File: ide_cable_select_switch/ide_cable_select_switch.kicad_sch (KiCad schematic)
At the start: 4 parts, among them J1 Conn_02x20_Odd_Even, J2 Conn_02x20_Odd_Even, J3 Conn_02x20_Odd_Even, SW1 SW_SPDT

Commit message: Updated headers in to specific IDE header without pad for key pin
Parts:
- J1, J2, J3: footprint Connector_PinHeader_2.54mm:PinHeader_2x20_P2.54mm_Vertical_SMD -> (none)
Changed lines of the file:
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@@
     (property "Reference" "J2" (id 0) (at 177.8 97.79 0))
     (property "Value" "Conn_02x20_Odd_Even" (id 1) (at 177.8 100.33 0))
-    (property "Footprint" "Connector_PinHeader_2.54mm:PinHeader_2x20_P2.54mm_Vertical_SMD" (id 2) (at 176.53 127 0)
+    (property "Footprint" "" (id 2) (at 176.53 127 0)
       (effects (font (size 1.27 1.27)) hide)
     )
@@
     (property "Reference" "J1" (id 0) (at 127 96.52 0))
     (property "Value" "Conn_02x20_Odd_Even" (id 1) (at 127 99.06 0))
-    (property "Footprint" "Connector_PinHeader_2.54mm:PinHeader_2x20_P2.54mm_Vertical_SMD" (id 2) (at 125.73 125.73 0)
+    (property "Footprint" "" (id 2) (at 125.73 125.73 0)
       (effects (font (size 1.27 1.27)) hide)
     )
@@
     (property "Reference" "J3" (id 0) (at 228.6 97.79 0))
     (property "Value" "Conn_02x20_Odd_Even" (id 1) (at 228.6 100.33 0))
-    (property "Footprint" "Connector_PinHeader_2.54mm:PinHeader_2x20_P2.54mm_Vertical_SMD" (id 2) (at 227.33 127 0)
+    (property "Footprint" "" (id 2) (at 227.33 127 0)
       (effects (font (size 1.27 1.27)) hide)
     )
@@
   (symbol_instances
     (path "/81a8578d-4991-432e-90c5-863c1508a25f"
-      (reference "J1") (unit 1) (value "Conn_02x20_Odd_Even") (footprint "Connector_PinHeader_2.54mm:PinHeader_2x20_P2.54mm_Vertical_SMD")
+      (reference "J1") (unit 1) (value "Conn_02x20_Odd_Even") (footprint "ide_cable_select_switch:IDE_ATA_Male_2x20_P2.54mm_Vertical_SMD")
     )
     (path "/2725ff94-5a7c-47c5-8447-1ffd34b9328e"
-      (reference "J2") (unit 1) (value "Conn_02x20_Odd_Even") (footprint "Connector_PinHeader_2.54mm:PinHeader_2x20_P2.54mm_Vertical_SMD")
+      (reference "J2") (unit 1) (value "Conn_02x20_Odd_Even") (footprint "ide_cable_select_switch:IDE_ATA_Male_2x20_P2.54mm_Vertical_SMD")
     )
     (path "/d0fe8934-21c4-4e46-b5b6-40801fb05422"
-      (reference "J3") (unit 1) (value "Conn_02x20_Odd_Even") (footprint "Connector_PinHeader_2.54mm:PinHeader_2x20_P2.54mm_Vertical_SMD")
+      (reference "J3") (unit 1) (value "Conn_02x20_Odd_Even") (footprint "ide_cable_select_switch:IDE_ATA_Male_2x20_P2.54mm_Vertical_SMD")
     )
     (path "/f84f0aad-79f2-4bd7-bb35-f56f8e0ea461"

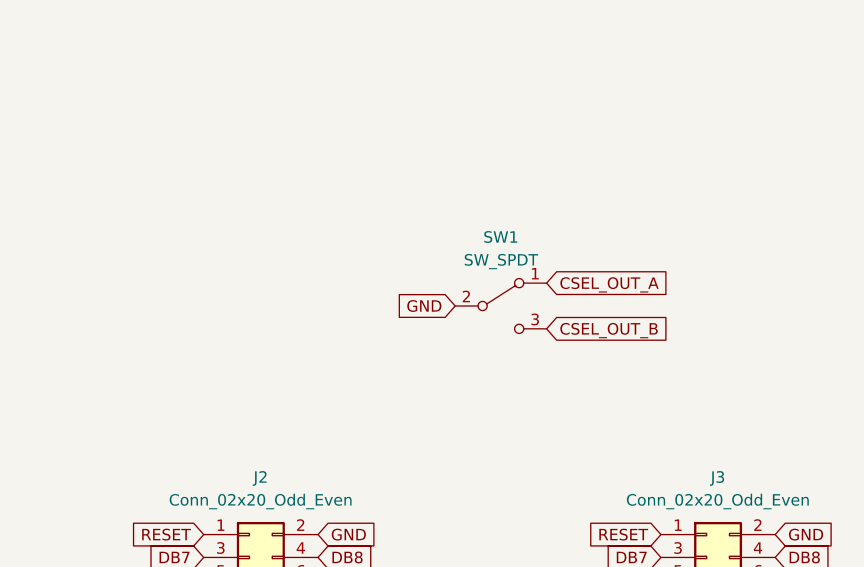
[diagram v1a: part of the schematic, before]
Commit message: Add pads for external switch
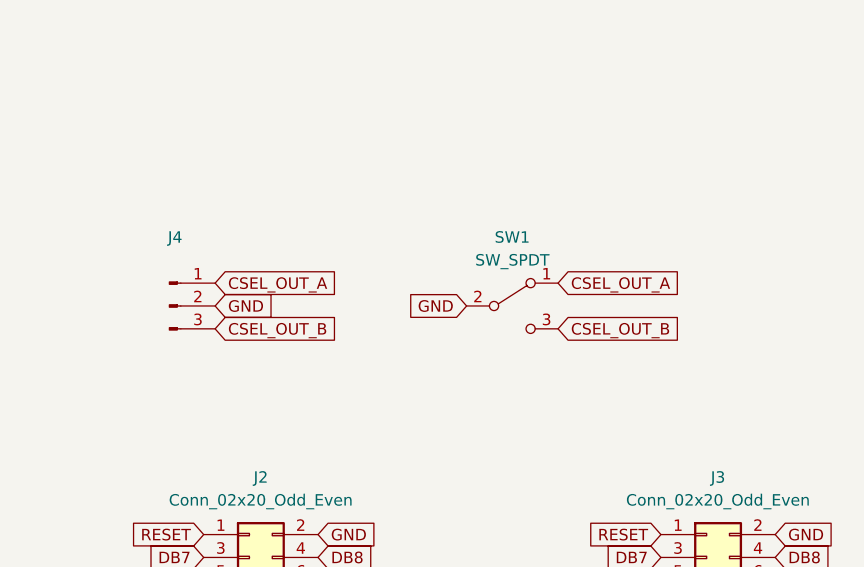
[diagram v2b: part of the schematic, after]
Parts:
- added J4: (no value), symbol Connector:Conn_01x03_Male
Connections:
- net CSEL_OUT_A: now also J4.1 (Pin_1)
- net CSEL_OUT_B: now also J4.3 (Pin_3)
- net GND: now also J4.2 (Pin_2)
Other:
- moved on the sheet: SW1
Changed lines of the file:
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@@
     )
   )
-  (global_label "CSEL_OUT_A" (shape input) (at 209.55 76.2 0) (fields_autoplaced)
-    (effects (font (size 1.27 1.27)) (justify left))
-    (property "Intersheet References" "${INTERSHEET_REFS}" (id 0) (at 223.2721 76.1206 0)
+  (global_label "CSEL_OUT_A" (shape input) (at 210.82 76.2 0) (fields_autoplaced)
+    (effects (font (size 1.27 1.27)) (justify left))
+    (property "Intersheet References" "${INTERSHEET_REFS}" (id 0) (at 224.5421 76.1206 0)
       (effects (font (size 1.27 1.27)) (justify left) hide)
     )
@@
     )
   )
+  (global_label "CSEL_OUT_B" (shape input) (at 210.82 81.28 0) (fields_autoplaced)
+    (effects (font (size 1.27 1.27)) (justify left))
+    (property "Intersheet References" "${INTERSHEET_REFS}" (id 0) (at 224.7236 81.2006 0)
+      (effects (font (size 1.27 1.27)) (justify left) hide)
+    )
+  )
+  (global_label "CSEL_OUT_A" (shape input) (at 172.72 76.2 0) (fields_autoplaced)
+    (effects (font (size 1.27 1.27)) (justify left))
+    (property "Intersheet References" "${INTERSHEET_REFS}" (id 0) (at 186.4421 76.1206 0)
+      (effects (font (size 1.27 1.27)) (justify left) hide)
+    )
+  )
   (global_label "GND" (shape input) (at 234.95 134.62 0) (fields_autoplaced)
     (effects (font (size 1.27 1.27)) (justify left))
@@
     )
   )
-  (global_label "CSEL_OUT_B" (shape input) (at 209.55 81.28 0) (fields_autoplaced)
-    (effects (font (size 1.27 1.27)) (justify left))
-    (property "Intersheet References" "${INTERSHEET_REFS}" (id 0) (at 223.4536 81.2006 0)
+  (global_label "CSEL_OUT_B" (shape input) (at 172.72 81.28 0) (fields_autoplaced)
+    (effects (font (size 1.27 1.27)) (justify left))
+    (property "Intersheet References" "${INTERSHEET_REFS}" (id 0) (at 186.6236 81.2006 0)
       (effects (font (size 1.27 1.27)) (justify left) hide)
     )
@@
     )
   )
-  (global_label "GND" (shape input) (at 199.39 78.74 180) (fields_autoplaced)
-    (effects (font (size 1.27 1.27)) (justify right))
-    (property "Intersheet References" "${INTERSHEET_REFS}" (id 0) (at 193.1064 78.6606 0)
+  (global_label "GND" (shape input) (at 200.66 78.74 180) (fields_autoplaced)
+    (effects (font (size 1.27 1.27)) (justify right))
+    (property "Intersheet References" "${INTERSHEET_REFS}" (id 0) (at 194.3764 78.6606 0)
       (effects (font (size 1.27 1.27)) (justify right) hide)
     )
@@
     (property "Intersheet References" "${INTERSHEET_REFS}" (id 0) (at 165.2874 124.3806 0)
       (effects (font (size 1.27 1.27)) (justify right) hide)
+    )
+  )
+  (global_label "GND" (shape input) (at 172.72 78.74 0) (fields_autoplaced)
+    (effects (font (size 1.27 1.27)) (justify left))
+    (property "Intersheet References" "${INTERSHEET_REFS}" (id 0) (at 179.0036 78.6606 0)
+      (effects (font (size 1.27 1.27)) (justify left) hide)
     )
   )
@@
     (pin "9")
   )
+  (symbol (lib_id "Connector:Conn_01x03_Male") (at 167.64 78.74 0) (unit 1)
+    (in_bom yes) (on_board yes) (fields_autoplaced)
+    (property "Reference" "J4" (id 0) (at 168.275 71.12 0))
+    (property "Value" "" (id 1) (at 168.275 73.66 0))
+    (property "Footprint" "" (id 2) (at 167.64 78.74 0)
+      (effects (font (size 1.27 1.27)) hide)
+    )
+    (property "Datasheet" "~" (id 3) (at 167.64 78.74 0)
+      (effects (font (size 1.27 1.27)) hide)
+    )
+    (pin "1")
+    (pin "2")
+    (pin "3")
+  )
   (symbol (lib_id "Connector_Generic:Conn_02x20_Odd_Even") (at 125.73 125.73 0) (unit 1)
     (in_bom yes) (on_board yes) (fields_autoplaced)
@@
     (pin "9")
   )
-  (symbol (lib_id "Switch:SW_SPDT") (at 204.47 78.74 0) (unit 1)
+  (symbol (lib_id "Switch:SW_SPDT") (at 205.74 78.74 0) (unit 1)
     (in_bom yes) (on_board yes) (fields_autoplaced)
-    (property "Reference" "SW1" (id 0) (at 204.47 71.12 0))
-    (property "Value" "SW_SPDT" (id 1) (at 204.47 73.66 0))
-    (property "Footprint" "Button_Switch_SMD:SW_SPDT_PCM12" (id 2) (at 204.47 78.74 0)
+    (property "Reference" "SW1" (id 0) (at 205.74 71.12 0))
+    (property "Value" "SW_SPDT" (id 1) (at 205.74 73.66 0))
+    (property "Footprint" "Button_Switch_SMD:SW_SPDT_PCM12" (id 2) (at 205.74 78.74 0)
       (effects (font (size 1.27 1.27)) hide)
     )
-    (property "Datasheet" "~" (id 3) (at 204.47 78.74 0)
+    (property "Datasheet" "~" (id 3) (at 205.74 78.74 0)
       (effects (font (size 1.27 1.27)) hide)
     )
@@
       (reference "J3") (unit 1) (value "Conn_02x20_Odd_Even") (footprint "ide_cable_select_switch:IDE_ATA_Male_2x20_P2.54mm_Vertical_SMD")
     )
+    (path "/69a7c72f-a2fd-4c6e-b751-3c324ac2da42"
+      (reference "J4") (unit 1) (value "Conn_01x03_Male") (footprint "ide_cable_select_switch:PinHeader_1x03_P2.54mm_Edge_SMD")
+    )
     (path "/f84f0aad-79f2-4bd7-bb35-f56f8e0ea461"

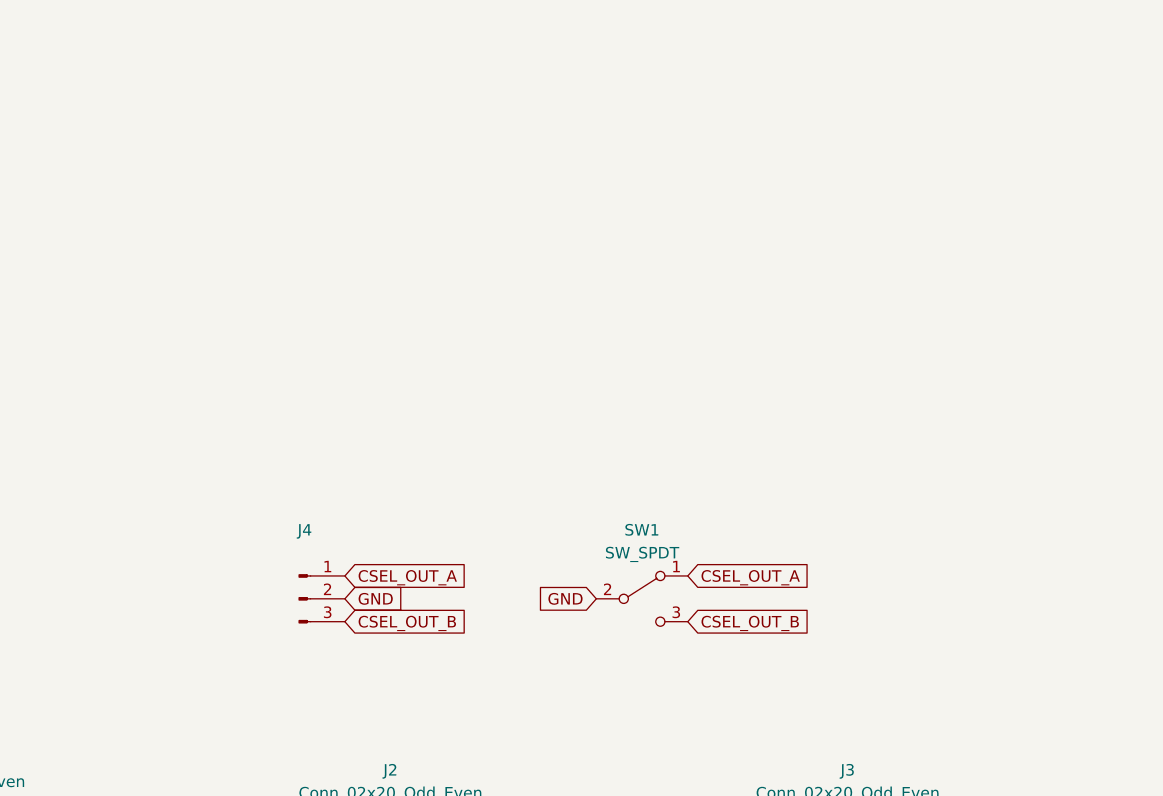
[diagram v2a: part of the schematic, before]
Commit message: Remove extra switch pads; turn main switch in to 2.54 header so it can be used for both a fixed and remote switch using the same footprint.
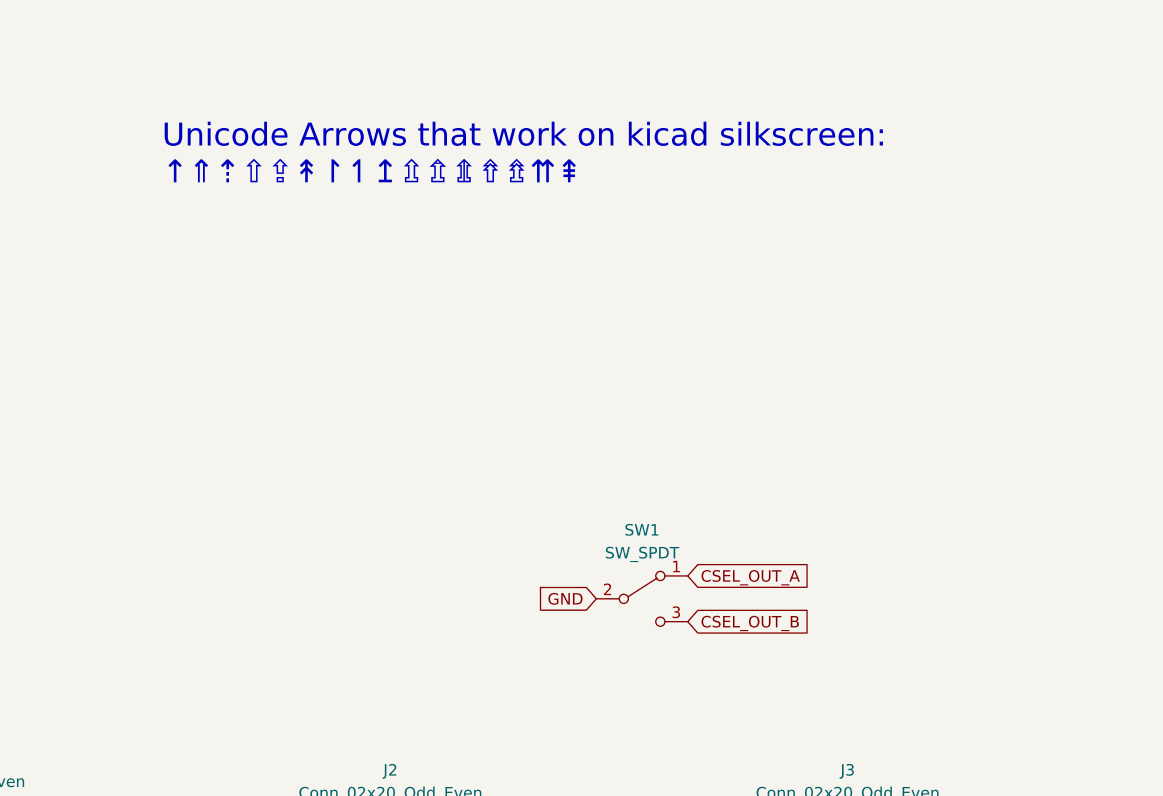
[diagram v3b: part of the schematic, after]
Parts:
- removed J4: (no value), symbol Connector:Conn_01x03_Male
- J1, J2, J3: footprint (none) -> ide_cable_select_switch:IDE_ATA_Male_2x20_P2.54mm_Vertical_SMD
- SW1: footprint Button_Switch_SMD:SW_SPDT_PCM12 -> (none)
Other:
- note added: "Unicode Arrows that work on kicad silkscreen: ↑⇑⇡︎⇧⇪↟↾↿↥⇫⇬⇭⇮⇯⇈⇞"
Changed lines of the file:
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@@
     (effects (font (size 1.27 1.27)) (justify left bottom))
+  )
+  (text "Unicode Arrows that work on kicad silkscreen:\n↑⇑⇡︎⇧⇪↟↾↿↥⇫⇬⇭⇮⇯⇈⇞"
+    (at 152.4 33.02 0)
+    (effects (font (size 2.54 2.54)) (justify left bottom))
   )
   (text "KEY" (at 133.985 127 0)
@@
     )
   )
-  (global_label "CSEL_OUT_A" (shape input) (at 172.72 76.2 0) (fields_autoplaced)
-    (effects (font (size 1.27 1.27)) (justify left))
-    (property "Intersheet References" "${INTERSHEET_REFS}" (id 0) (at 186.4421 76.1206 0)
-      (effects (font (size 1.27 1.27)) (justify left) hide)
-    )
-  )
   (global_label "GND" (shape input) (at 234.95 134.62 0) (fields_autoplaced)
     (effects (font (size 1.27 1.27)) (justify left))
@@
     )
   )
-  (global_label "CSEL_OUT_B" (shape input) (at 172.72 81.28 0) (fields_autoplaced)
-    (effects (font (size 1.27 1.27)) (justify left))
-    (property "Intersheet References" "${INTERSHEET_REFS}" (id 0) (at 186.6236 81.2006 0)
-      (effects (font (size 1.27 1.27)) (justify left) hide)
-    )
-  )
   (global_label "GND" (shape input) (at 120.65 125.73 180) (fields_autoplaced)
     (effects (font (size 1.27 1.27)) (justify right))
@@
     (property "Intersheet References" "${INTERSHEET_REFS}" (id 0) (at 165.2874 124.3806 0)
       (effects (font (size 1.27 1.27)) (justify right) hide)
-    )
-  )
-  (global_label "GND" (shape input) (at 172.72 78.74 0) (fields_autoplaced)
-    (effects (font (size 1.27 1.27)) (justify left))
-    (property "Intersheet References" "${INTERSHEET_REFS}" (id 0) (at 179.0036 78.6606 0)
-      (effects (font (size 1.27 1.27)) (justify left) hide)
     )
   )
@@
     (property "Reference" "J2" (id 0) (at 177.8 97.79 0))
     (property "Value" "Conn_02x20_Odd_Even" (id 1) (at 177.8 100.33 0))
-    (property "Footprint" "" (id 2) (at 176.53 127 0)
+    (property "Footprint" "ide_cable_select_switch:IDE_ATA_Male_2x20_P2.54mm_Vertical_SMD" (id 2) (at 176.53 127 0)
       (effects (font (size 1.27 1.27)) hide)
     )
@@
     (pin "9")
   )
-  (symbol (lib_id "Connector:Conn_01x03_Male") (at 167.64 78.74 0) (unit 1)
-    (in_bom yes) (on_board yes) (fields_autoplaced)
-    (property "Reference" "J4" (id 0) (at 168.275 71.12 0))
-    (property "Value" "" (id 1) (at 168.275 73.66 0))
-    (property "Footprint" "" (id 2) (at 167.64 78.74 0)
-      (effects (font (size 1.27 1.27)) hide)
-    )
-    (property "Datasheet" "~" (id 3) (at 167.64 78.74 0)
-      (effects (font (size 1.27 1.27)) hide)
-    )
-    (pin "1")
-    (pin "2")
-    (pin "3")
-  )
   (symbol (lib_id "Connector_Generic:Conn_02x20_Odd_Even") (at 125.73 125.73 0) (unit 1)
     (in_bom yes) (on_board yes) (fields_autoplaced)
     (property "Reference" "J1" (id 0) (at 127 96.52 0))
     (property "Value" "Conn_02x20_Odd_Even" (id 1) (at 127 99.06 0))
-    (property "Footprint" "" (id 2) (at 125.73 125.73 0)
+    (property "Footprint" "ide_cable_select_switch:IDE_ATA_Male_2x20_P2.54mm_Vertical_SMD" (id 2) (at 125.73 125.73 0)
       (effects (font (size 1.27 1.27)) hide)
     )
@@
     (property "Reference" "J3" (id 0) (at 228.6 97.79 0))
     (property "Value" "Conn_02x20_Odd_Even" (id 1) (at 228.6 100.33 0))
-    (property "Footprint" "" (id 2) (at 227.33 127 0)
+    (property "Footprint" "ide_cable_select_switch:IDE_ATA_Male_2x20_P2.54mm_Vertical_SMD" (id 2) (at 227.33 127 0)
       (effects (font (size 1.27 1.27)) hide)
     )
@@
     (property "Reference" "SW1" (id 0) (at 205.74 71.12 0))
     (property "Value" "SW_SPDT" (id 1) (at 205.74 73.66 0))
-    (property "Footprint" "Button_Switch_SMD:SW_SPDT_PCM12" (id 2) (at 205.74 78.74 0)
+    (property "Footprint" "" (id 2) (at 205.74 78.74 0)
       (effects (font (size 1.27 1.27)) hide)
     )
@@
       (reference "J3") (unit 1) (value "Conn_02x20_Odd_Even") (footprint "ide_cable_select_switch:IDE_ATA_Male_2x20_P2.54mm_Vertical_SMD")
     )
-    (path "/69a7c72f-a2fd-4c6e-b751-3c324ac2da42"
-      (reference "J4") (unit 1) (value "Conn_01x03_Male") (footprint "ide_cable_select_switch:PinHeader_1x03_P2.54mm_Edge_SMD")
-    )
     (path "/f84f0aad-79f2-4bd7-bb35-f56f8e0ea461"
-      (reference "SW1") (unit 1) (value "SW_SPDT") (footprint "Button_Switch_SMD:SW_SPDT_PCM12")
-    )
-  )
+      (reference "SW1") (unit 1) (value "SW_SPDT") (footprint "Connector_PinHeader_2.54mm:PinHeader_1x03_P2.54mm_Vertical")
+    )
+  )

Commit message: previous fab changes
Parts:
- SW1: footprint (none) -> Connector_PinHeader_2.54mm:PinHeader_1x03_P2.54mm_Vertical
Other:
- note added: "11/2022"
- note added: "Change IDE Master/Slave without jumpers or moving position on cable."
- note added: "IDE Cable Select Switch"
- note added: "IDE cable select switch"
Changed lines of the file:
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@@
     (effects (font (size 1.27 1.27)) (justify left bottom))
   )
+  (text "IDE cable select switch" (at 187.96 190.5 0)
+    (effects (font (size 2.54 2.54)) (justify left bottom))
+  )
+  (text "IDE Cable Select Switch" (at 177.8 172.72 0)
+    (effects (font (size 2.54 2.54)) (justify left bottom))
+  )
+  (text "Change IDE Master/Slave without jumpers or moving position on cable."
+    (at 177.8 177.8 0)
+    (effects (font (size 1.27 1.27)) (justify left bottom))
+  )
   (text "KEY" (at 235.585 128.27 0)
+    (effects (font (size 1.27 1.27)) (justify left bottom))
+  )
+  (text "11/2022" (at 208.28 193.04 0)
     (effects (font (size 1.27 1.27)) (justify left bottom))
   )
@@
     (property "Reference" "SW1" (id 0) (at 205.74 71.12 0))
     (property "Value" "SW_SPDT" (id 1) (at 205.74 73.66 0))
-    (property "Footprint" "" (id 2) (at 205.74 78.74 0)
+    (property "Footprint" "Connector_PinHeader_2.54mm:PinHeader_1x03_P2.54mm_Vertical" (id 2) (at 205.74 78.74 0)
       (effects (font (size 1.27 1.27)) hide)
     )
